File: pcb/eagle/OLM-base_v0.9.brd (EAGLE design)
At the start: 94.7 x 56.5 mm, 33 parts, among them IC1 ATMEGA, IC2 MCP1702-33, IC3 ENC28J60SP, J1 MAGJACK, J2 POWER_JACKPTH, X1 16 MHz, X3 25MHz

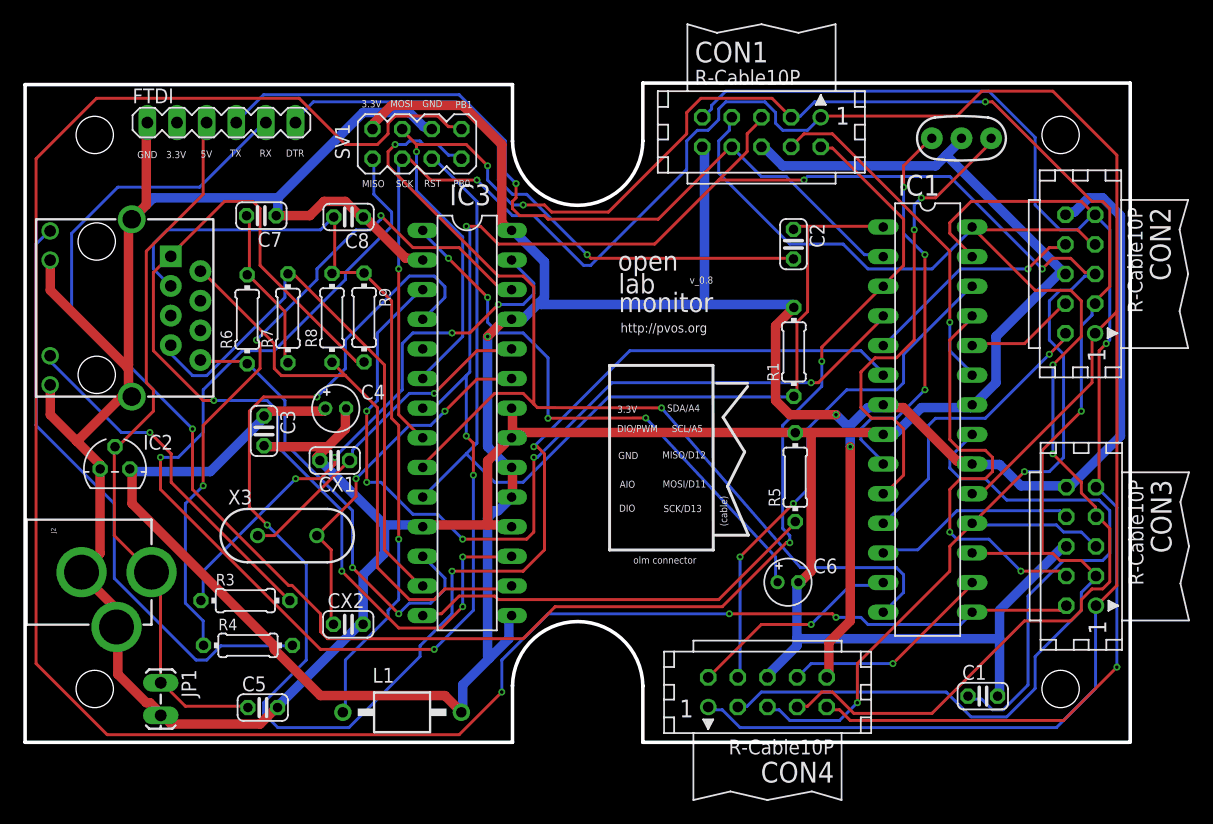
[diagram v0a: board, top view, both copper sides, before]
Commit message: changed output for smart-prototyping
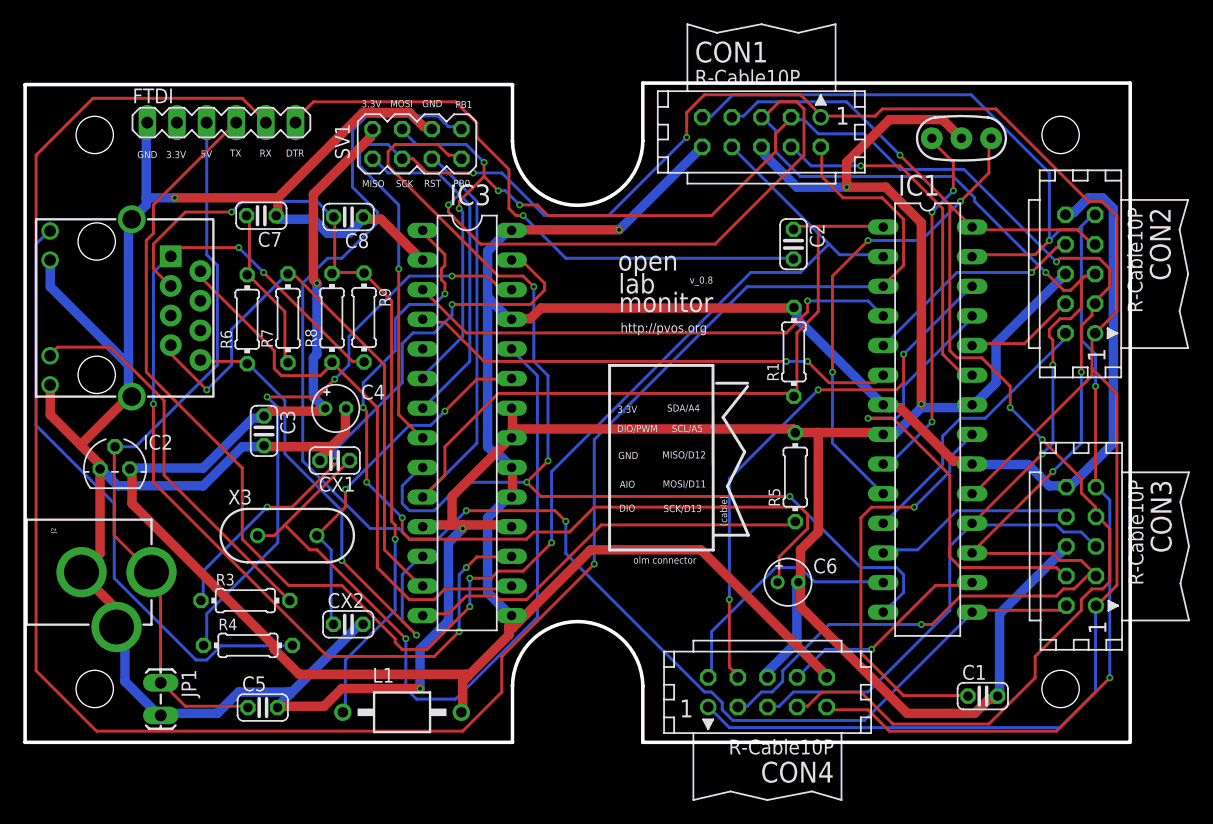
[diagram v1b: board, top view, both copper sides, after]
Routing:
- net D4: track 133.7 -> 42.1 mm, vias 4 -> 2
- net MISO/D12: track 248.7 -> 175.0 mm, vias 9 -> 4
- net D0/RX: track 70.7 -> 133.0 mm, vias 1 -> 3
- net PB1/D9/PWM: track 183.3 -> 125.6 mm, vias 3 -> 2
- net GND: track 339.2 -> 382.7 mm, vias 0 -> 5
- net N$52: track 28.7 -> 67.7 mm
- net D2: track 76.6 -> 43.2 mm, vias 5 -> 1
- net D1/TX: track 149.6 -> 183.0 mm, vias 3 -> 1
- net N$50: track 48.8 -> 75.8 mm
- net VCC: track 260.3 -> 273.5 mm, vias 3 -> 2
- net SDA/A4: track 128.9 -> 117.9 mm, vias 2 -> 3
- net N$19: track 45.2 -> 35.5 mm, vias 0 -> 1
- net MOSI/D11: track 180.8 -> 171.3 mm, vias 5 -> 8
- net PB0/D8: track 90.3 -> 98.5 mm, vias 2 -> 4
- net N$39: track 59.2 -> 51.5 mm
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
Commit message: fixed logo
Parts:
- removed R9: 49.9, rcl:0204/7
- added R2: 1K, rcl:0204/7
- J1: value MAGJACK -> POWER_JACKPTH; device SparkFun:MAGJACK -> SparkFun-Connectors:POWER_JACK_PTH
- J2: value POWER_JACKPTH -> MAGJACK; device SparkFun-Connectors:POWER_JACK_PTH -> SparkFun:MAGJACK
- R4: value 1K -> 2.32K
- R5: value 2.32K -> 49.9
- moved R4 51.9 mm to (68.5, 24.0), turned to 90 degrees
- moved R5 48.0 mm to (19.8, 35.6)
- moved J1 30.3 mm to (-2.89, 14.5)
- moved J2 30.3 mm to (-4.98, 44.8)
- moved C4 6.46 mm to (22.3, 23.8)
- moved C3 4.93 mm to (16.3, 24.0), turned to 180 degrees
- moved R7 4.40 mm to (26.8, 35.6)
- moved R3 3.85 mm to (19.1, 8.27)
- moved R6 3.33 mm to (22.3, 35.5)
- moved C6 3.31 mm to (68.2, 15.5)
- moved R8 3.26 mm to (29.4, 35.5), turned to 270 degrees
- moved C7 2.90 mm to (21.0, 42.3)
- moved R1 2.84 mm to (68.7, 33.9)
- moved C8 2.81 mm to (28.0, 42.2)
- moved C2 2.67 mm to (68.1, 41.2), turned to 0 degrees
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- renumbered X3 to X2
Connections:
- net GND: now also J1.GND, J1.GNDBREAK, J2.10, J2.12, J2.M1, J2.M2, R4.2; no longer J1.10, J1.12, J1.M1, J1.M2, J2.GND, J2.GNDBREAK, R5.2
- net LEDA: now also J2.11, R2.2; no longer J1.11, R3.2
- net LEDB: now also J2.9, R3.2; no longer J1.9, R4.2
- net MISO/D12: now also IC3.6; no longer IC3.7
- net MOSI/D11: now also IC3.7; no longer IC3.6
- net N$37: now also R2.1; no longer R3.1
- net N$39: now also R3.1; no longer R4.1
- net N$51: now also R4.1; no longer R5.1
- net N$54: now also R5.2, R6.1; no longer R6.2, R7.1
- net RD+: now also J2.7, R6.2; no longer J1.7, R7.2
- net RD-: now also J2.8, R5.1; no longer J1.8, R6.1
- net TCT: now also J2.3, R7.2, R8.1; no longer J1.3, R8.2, R9.1
- net TD+: now also J2.1, R8.2; no longer J1.1, R9.2
- net TD-: now also J2.2, R7.1; no longer J1.2, R8.1
- net VIN: now also J1.PWR; no longer J2.PWR
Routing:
- net N$20: track 51.9 -> 123.5 mm, vias 1 -> 5
- net D0/RX: track 133.0 -> 75.9 mm, vias 3 -> 4
- net GND: track 382.7 -> 339.4 mm, vias 5 -> 0
- net D1/TX: track 183.0 -> 141.5 mm, vias 1 -> 4
- net N$52: track 67.7 -> 28.4 mm, vias 1 -> 2
- net VCC: track 273.5 -> 237.9 mm
- net N$21: track 40.6 -> 74.1 mm, vias 3 -> 6
- net TD+: track 84.3 -> 51.8 mm, vias 5 -> 1
- net N$50: track 75.8 -> 46.6 mm, vias 4 -> 1
- net PB1/D9/PWM: track 125.6 -> 98.4 mm, vias 2 -> 3
- net A3: track 46.4 -> 64.8 mm, vias 3 -> 4
- net N$1: track 31.5 -> 46.6 mm, vias 3 -> 4
- net MISO/D12: track 175.0 -> 189.7 mm
- net MOSI/D11: track 171.3 -> 184.7 mm, vias 8 -> 6
- net D4: track 42.1 -> 53.7 mm, vias 2 -> 4
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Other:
- board text added: "BATT"
- board text added: "X1"
- board text added: "olm_1"
- board text added: "olm_2"
- board text added: "olm_3"
- board text added: "olm_4"
- board text added: "olm_connector"
- board text added: "v0.9"
- board text removed: "olm connector"
- board text removed: "v_0.8"
